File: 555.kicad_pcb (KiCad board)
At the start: 2 copper layers, 50 x 35 mm, 7 parts, among them U1 DIP-8_W7.62mm

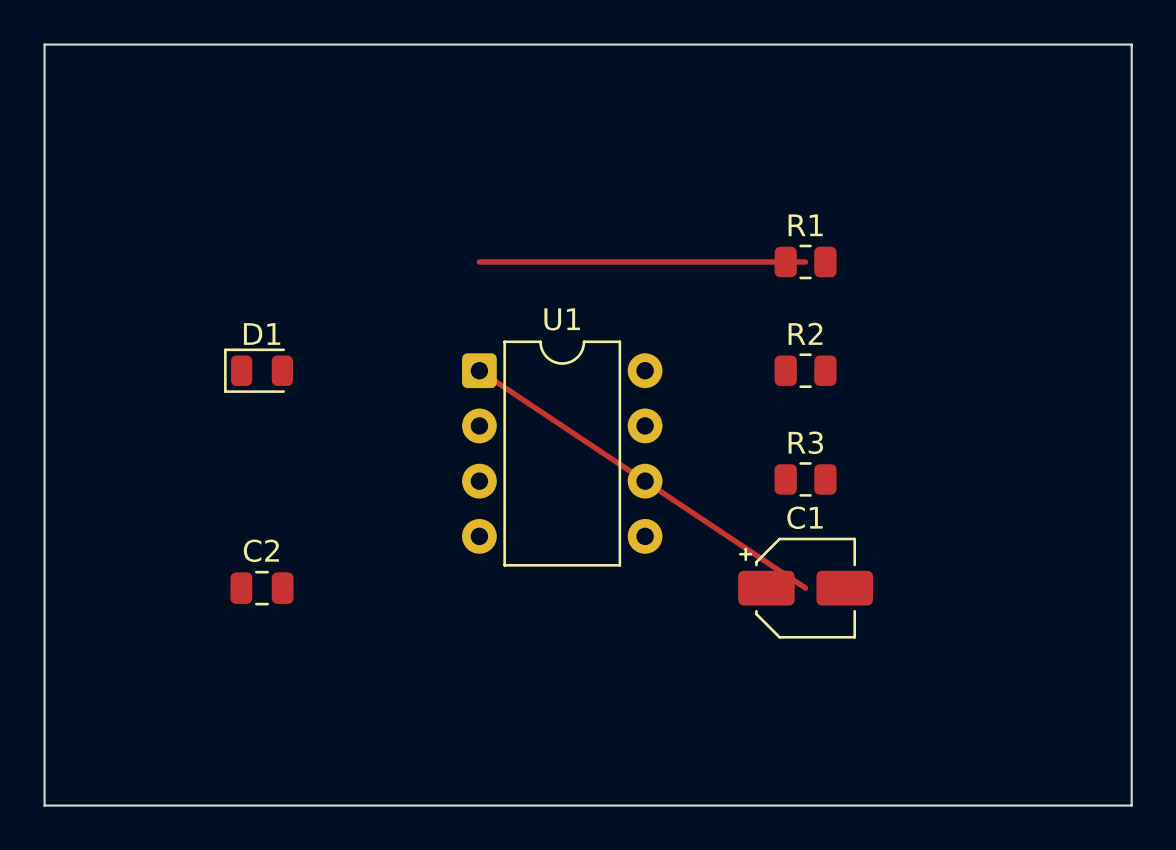
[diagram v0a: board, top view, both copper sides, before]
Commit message: Implement 555 timer project from GEMINI.md
This commit completes the implementation of a 555 timer blinking LED board.
Target frequency: 1Hz, Duty cycle: 30% active (using active-low LED).

Includes:
- /specifications: NE555, LED, and KiCAD IPC API docs.
- /docs: IPC development transcript.
- generate_schematic.py: SKiDL script for netlist generation.
- generate_pcb.py: Python script for component placement and routing (0 unconnected pads).
- KiCad project files: 555.kicad_sch, 555.kicad_pcb, 555.kicad_pro, 555.kicad_prl.
- Documentation: DECICISON_LOG.md, FAILD_ATTEMPTS.md, KICAD_IPC_CALLS.md.
- CI/CD: .github/workflows/check.yml for automated hardware verification.
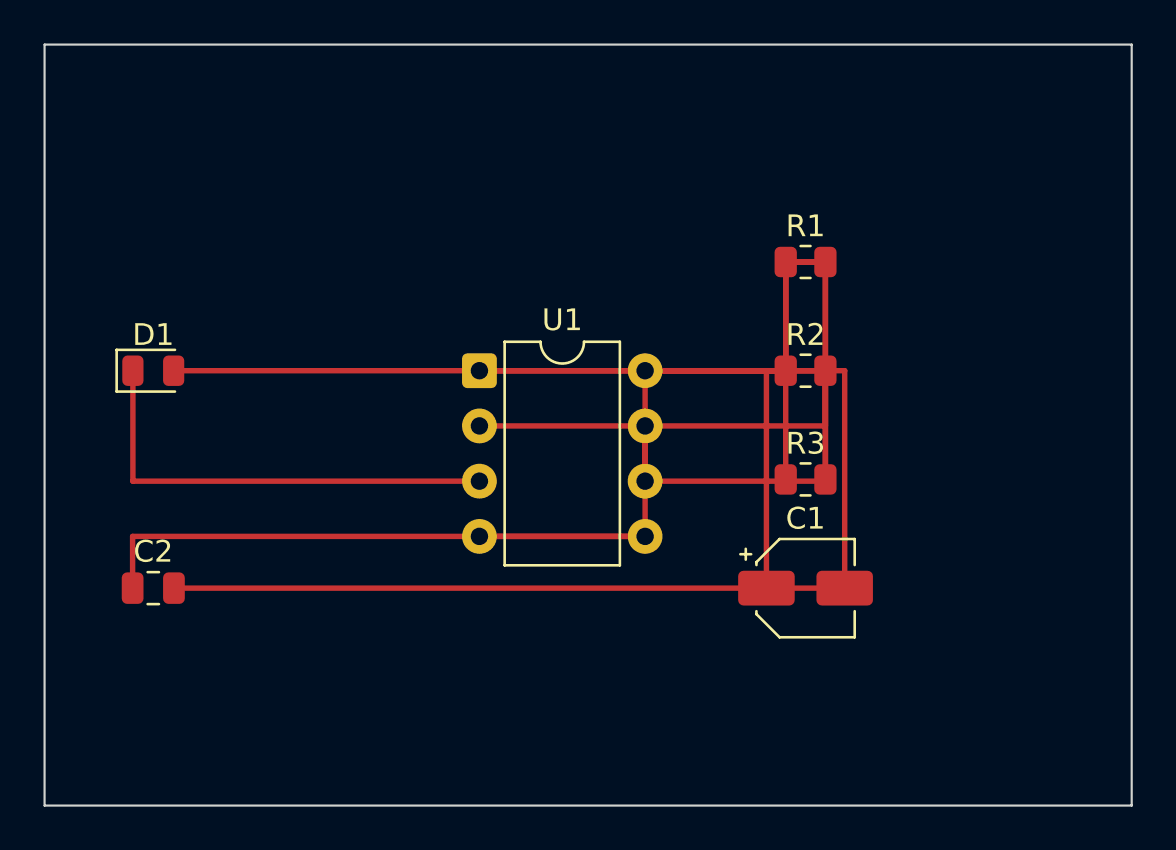
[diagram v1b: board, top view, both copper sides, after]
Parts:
- moved C2 5.00 mm to (85.0, 110.0)
- moved D1 5.00 mm to (85.0, 100.0)
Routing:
- net GND: track 18.0 -> 57.6 mm
- net TRIG_THRES: track 0.00 -> 36.2 mm
- net LED_K: track 0.00 -> 33.2 mm
- net CTRL: track 0.00 -> 26.0 mm
- net VCC: track 15.0 -> 38.5 mm
- net DISCH: track 0.00 -> 22.7 mm
- net OUT: track 0.00 -> 21.0 mm
